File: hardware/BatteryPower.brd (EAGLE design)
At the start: 47 x 40.5 mm, 36 parts, among them U1 CH004-2032LF, U2 ACS711ELCTR-12AB-T, U3 ACS711ELCTR-12AB-T

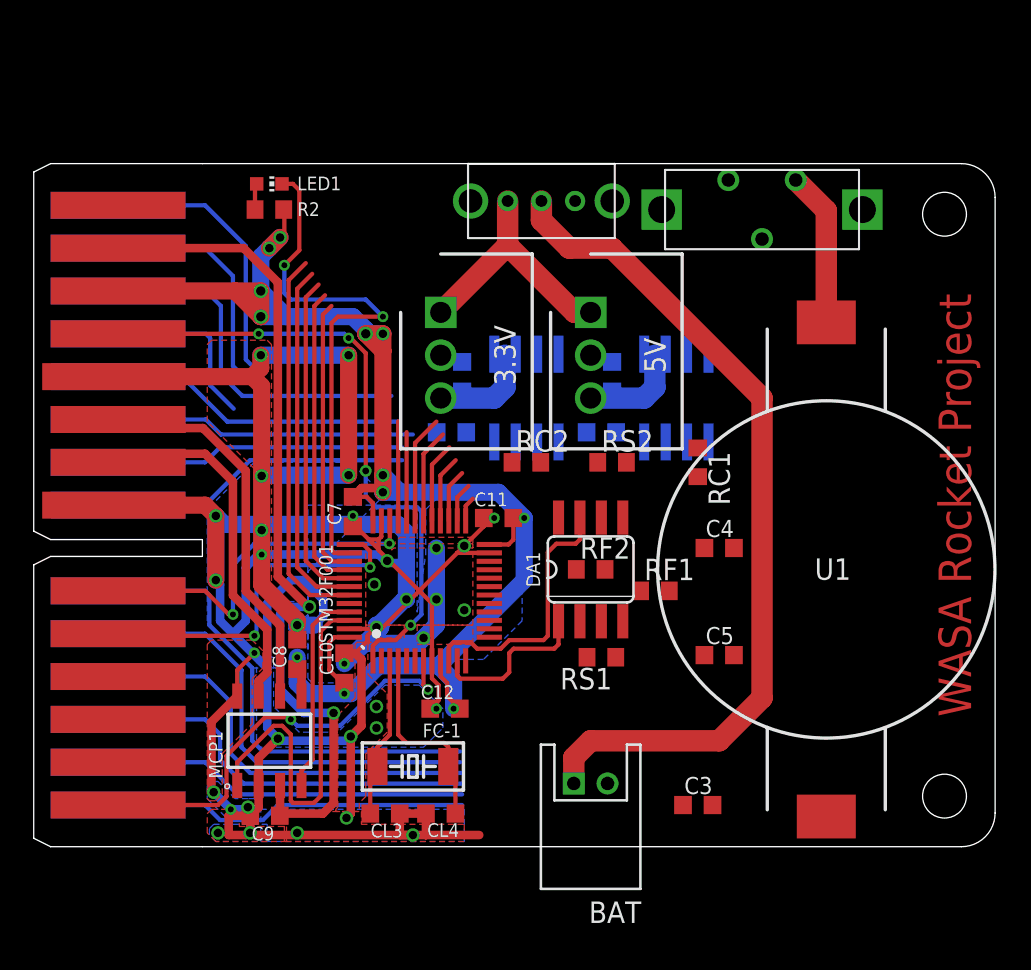
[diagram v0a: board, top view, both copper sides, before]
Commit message: Layout battery power board
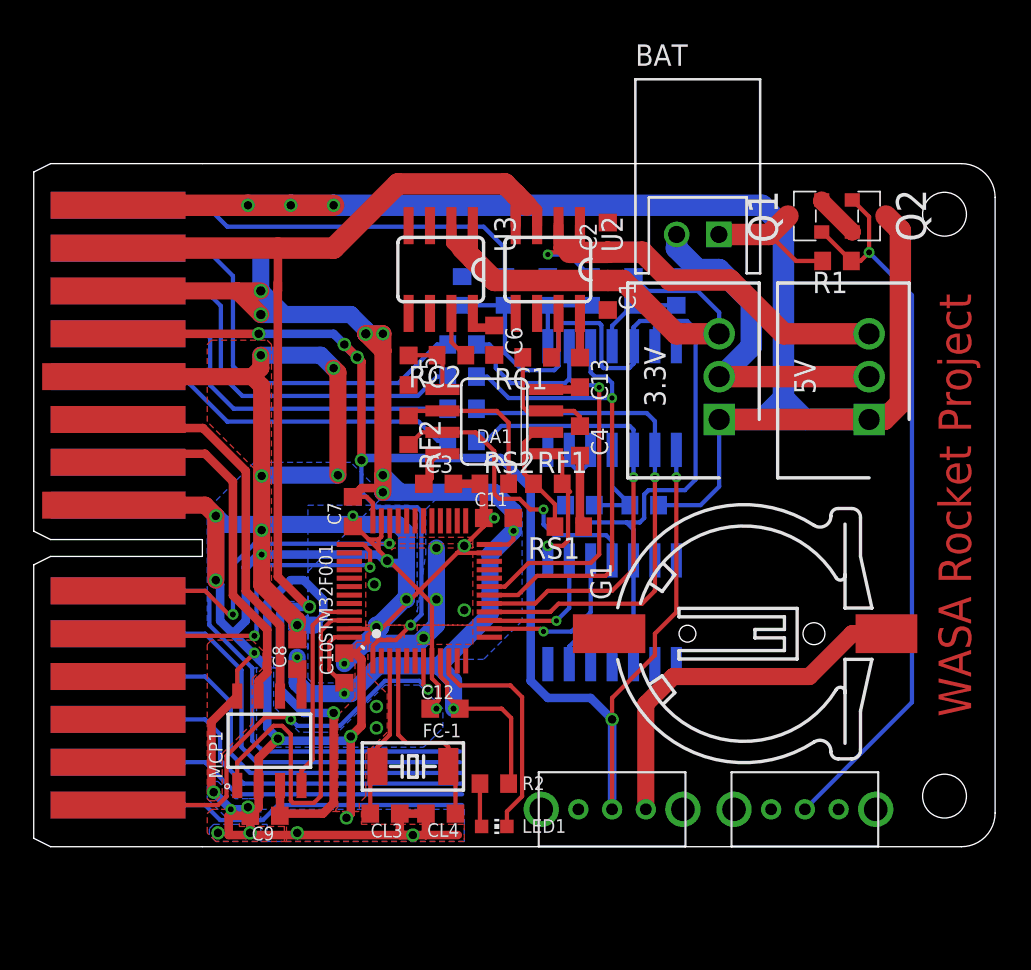
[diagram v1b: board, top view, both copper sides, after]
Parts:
- removed U$3: ESD175202, switches:ESD175202
- removed U1: CH004-2032LF, CH004-2032LF:CH004-2032LF
- added G1: CH291-1220LF, battery:CH291-1220LF
- added IC1, IC2: 4066D, 40xx:SO14
- added Q1, Q2: IRLML5203, transistor-power:MICRO3
- added R1: 100k, rcl:R0603
- added R10, R3, R5, R6, R7, R8: 10k, rcl:R0603
- added R11, R12, R13, R14, R4, R9: 1k, rcl:R0603
- added U$4: SK-12D01-VG4, switches:SK-12D01-VG4
- BAT: device jst-ph:S2B-PH-K-S -> con-jst-xh:S2B-XH-A
- moved LED1 40.4 mm to (27.3, -19.1)
- moved U$1 39.3 mm to (45.7, -18.0)
- moved R2 36.6 mm to (27.3, -16.5)
- moved BAT 33.2 mm to (39.4, 16.0), turned to 0 degrees
- moved C5 25.0 mm to (22.2, 8.00), turned to 270 degrees
- moved C3 24.5 mm to (24.0, 1.27)
- moved 3.3V 17.7 mm to (40.6, 5.08), turned to 90 degrees
- moved 5V 17.7 mm to (49.5, 5.08), turned to 90 degrees
- moved RF2 13.6 mm to (22.2, 4.45), turned to 270 degrees
- moved RC1 11.4 mm to (29.8, 8.76), turned to 180 degrees
- moved U2 10.8 mm to (30.5, 14.0), flipped to the top
- moved DA1 10.5 mm to (27.3, 4.95), turned to 90 degrees
- moved C4 10.4 mm to (32.4, 3.81), turned to 270 degrees
- moved C1 9.89 mm to (34.0, 12.4), flipped to the top, turned to 270 degrees
- moved U3 9.16 mm to (24.1, 14.0), flipped to the top
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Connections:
- net N$2 renamed 5VC'
- net N$3 renamed 3.3VC'
- removed net I2C1_SCK: STM32F001.43
- removed net I2C1_SCL: STM32F001.42
- removed net N$11: U$3.B, U1.1
- removed net N$53: STM32F001.12
- removed net N$54: STM32F001.13
- removed net N$55: STM32F001.14
- removed net N$56: STM32F001.15
- removed net N$57: STM32F001.16
- removed net N$58: STM32F001.17
- removed net N$59: STM32F001.29
- removed net N$60: STM32F001.32
- removed net N$61: STM32F001.33
- removed net N$62: STM32F001.18
- removed net N$63: STM32F001.19
- removed net N$64: STM32F001.20
- removed net N$65: STM32F001.21
- removed net N$66: STM32F001.22
- removed net N$67: STM32F001.25
- removed net N$68: STM32F001.26
- removed net N$69: STM32F001.27
- removed net N$70: STM32F001.28
- removed net N$74: U$2.16
- removed net SPI1_MISO: STM32F001.40
- removed net SPI1_MOSI: STM32F001.41
- removed net SPI1_SCK: STM32F001.39
- removed net USART1_RX: STM32F001.31
- removed net USART1_TX: STM32F001.30
- new net !HIL!: IC1.12, IC1.13, IC1.5, IC1.6, IC2.13, IC2.5, R10.1, R9.1
- new net BAT+: BAT.1, Q1.3, R1.2
- new net BU+: G1.+, U$4.B
- new net N$2: Q1.2, Q2.2
- new net POWER_CTRL: Q1.1, Q2.1, R1.1, U$1.C
- new net PVCC: IC1.8, R5.1, R6.2
- new net PVDD: IC1.11, R7.1, R8.2
- new net PVPP: IC1.4, R3.1, R4.2
- new net SCVCC: IC2.2, STM32F001.15
- new net SCVDD: IC2.3, STM32F001.14
- new net SVBU: IC1.2, R13.1, STM32F001.16
- new net SVCC: IC1.9, R11.1, STM32F001.19
- new net SVDD: IC1.10, R12.1, STM32F001.18
- new net SVPP: IC1.3, R14.1, STM32F001.17
- net 3.3V: now also R7.2
- net 3.3VC: now also IC2.4; no longer STM32F001.10
- net 5V: now also R5.2
- net 5VC: now also IC2.1; no longer STM32F001.11
- net GND: now also G1.-, IC1.7, IC2.7, R4.1, R6.1, R8.1, U$1.B; no longer U1.2
- net N$1: now also R9.2, U$2.16; no longer 3.3V.1, 5V.1, U$1.B
- net N$48: now also R14.2
- net N$49: now also R13.2
- net N$50: now also R12.2
- net N$73: now also STM32F001.10; no longer STM32F001.38
- net N$75: now also R11.2
- net VBAT: now also IC1.1, U$4.C; no longer U$3.C
- net VDD: now also IC1.14, IC2.14, R10.2
- net VPP: now also 3.3V.1, 5V.1, Q2.3, R3.2; no longer BAT.1, U$1.C
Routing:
- net !HIL!: track 0.00 -> 61.9 mm
- net VBAT: track 38.0 -> 94.9 mm, vias 4 -> 7
- net VPP: track 50.5 -> 102.1 mm, vias 0 -> 3
- net POWER_CTRL: track 0.00 -> 44.0 mm, vias 0 -> 1
- net SVBU: track 0.00 -> 31.3 mm, vias 0 -> 1
- net SVDD: track 0.00 -> 30.6 mm, vias 0 -> 1
- net SVCC: track 0.00 -> 28.3 mm, vias 0 -> 1
- net GND: track 213.4 -> 241.1 mm
- net SVPP: track 0.00 -> 27.4 mm, vias 0 -> 1
- net I2C1_SCK: track 23.0 -> 0.00 mm
- net 5V: track 5.98 -> 28.5 mm, vias 0 -> 1
- net 3.3V: track 5.98 -> 28.4 mm
- net BU+: track 0.00 -> 22.2 mm
- net VCC: track 51.1 -> 73.2 mm
- net I2C1_SCL: track 21.3 -> 0.00 mm
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
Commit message: Complete battery power board
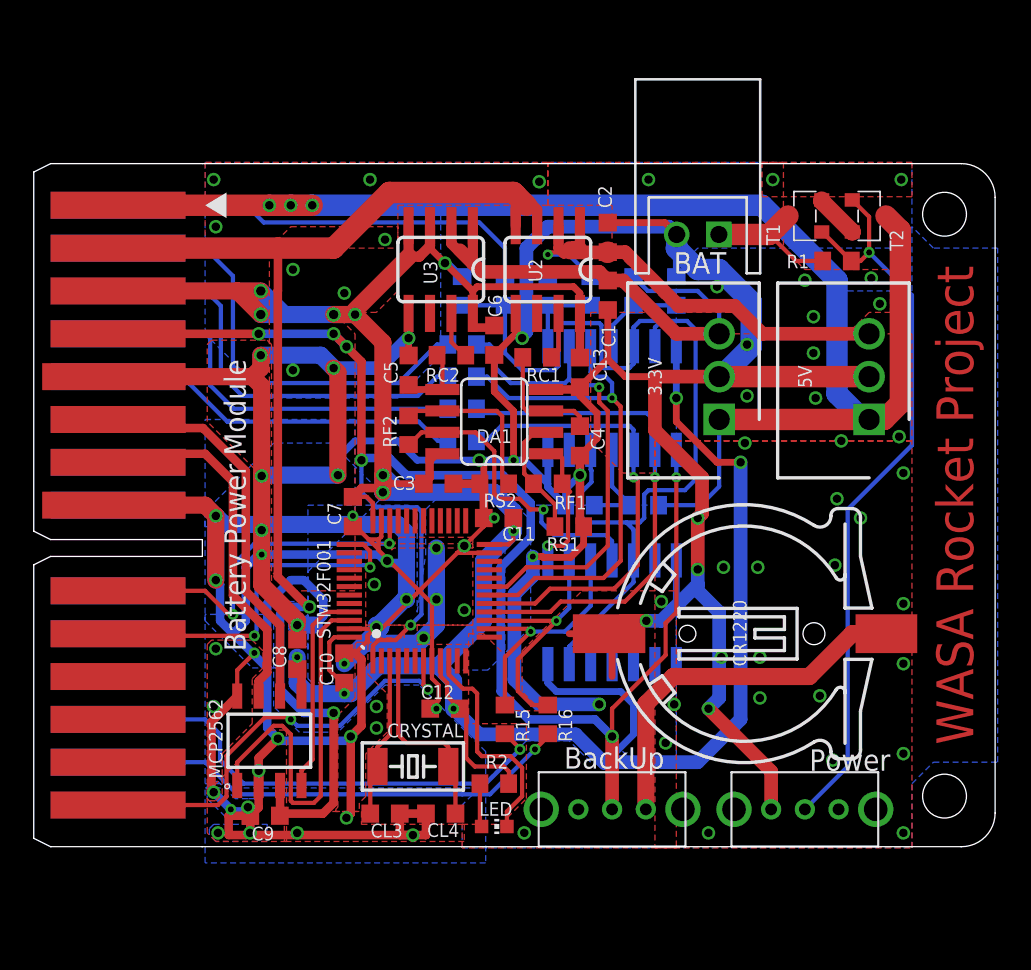
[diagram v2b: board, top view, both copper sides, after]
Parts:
- added R15, R16: 1k, resistor:R0603
- turned C5 to 90 degrees
- renumbered FC-1 to CRYSTAL, G1 to CR1220, LED1 to LED, MCP1 to MCP2562, Q1 to T1, Q2 to T2, U$4 to BACKUP
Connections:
- removed net N$33: U$2.30
- removed net N$36: U$2.27
- removed net N$43: U$2.26
- removed net N$44: U$2.25
- removed net N$45: U$2.23
- removed net N$46: U$2.22
- removed net N$47: U$2.21
- net N$34: now also R16.2
- net N$35: now also R15.2
- net SCVCC: now also R16.1
- net SCVDD: now also R15.1
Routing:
- net GND: track 241.1 -> 381.6 mm, vias 35 -> 91
- net VDD: track 103.1 -> 179.8 mm, vias 10 -> 13
- net N$44: track 27.8 -> 0.00 mm
- net N$43: track 26.1 -> 0.00 mm
- net N$36: track 24.6 -> 0.00 mm
- net N$33: track 21.1 -> 0.00 mm
- net VPP: track 102.1 -> 86.9 mm
- net SCVCC: track 7.89 -> 15.1 mm
- net N$34: track 21.2 -> 27.9 mm, vias 0 -> 1
- net N$35: track 22.9 -> 28.4 mm, vias 0 -> 1
- net SCVDD: track 9.62 -> 14.4 mm
- net VBAT: track 94.9 -> 92.3 mm
- net VCC: track 73.2 -> 72.3 mm
- net SVBU: track 31.3 -> 30.6 mm
- net !HIL!: track 61.9 -> 61.3 mm
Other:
- board text added: "BackUp"
- board text added: "Battery Power Module"
- board text added: "Designed by @fujiy0, 2019"
- board text added: "Power"

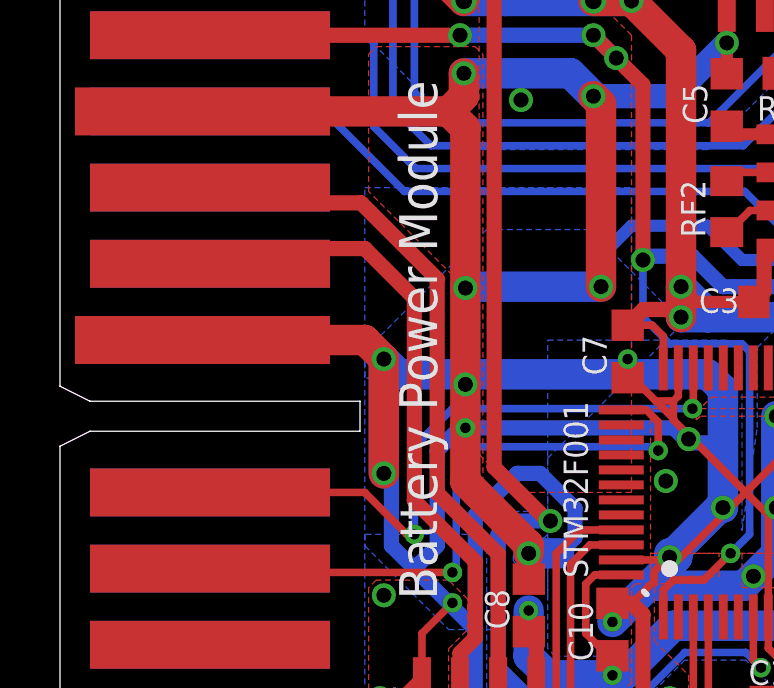
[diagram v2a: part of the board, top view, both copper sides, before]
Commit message: Clean silk print
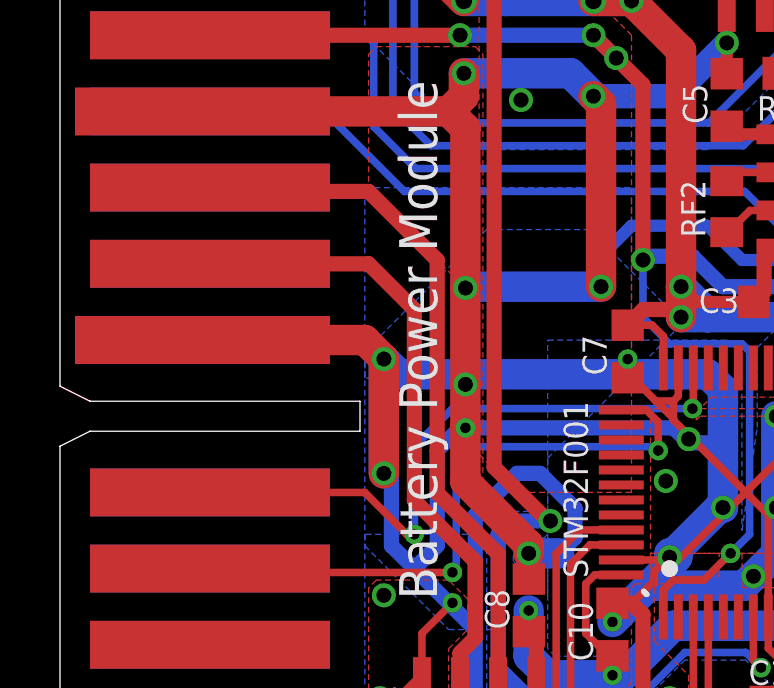
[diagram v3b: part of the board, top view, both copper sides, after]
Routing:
- net CANH1: track 21.5 -> 20.8 mm
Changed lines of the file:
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@@
 <layer number="28" name="bValues" color="7" fill="1" visible="no" active="yes"/>
 <layer number="29" name="tStop" color="7" fill="3" visible="no" active="yes"/>
-<layer number="30" name="bStop" color="7" fill="6" visible="yes" active="yes"/>
+<layer number="30" name="bStop" color="7" fill="6" visible="no" active="yes"/>
 <layer number="31" name="tCream" color="7" fill="4" visible="no" active="yes"/>
 <layer number="32" name="bCream" color="7" fill="5" visible="no" active="yes"/>
@@
 <contactref element="U$2" pad="7"/>
 <contactref element="MCP2562" pad="7"/>
-<wire x1="11.811" y1="1.397" x2="11.811" y2="-5.351" width="0.508" layer="1"/>
+<wire x1="11.811" y1="1.016" x2="11.811" y2="-5.351" width="0.508" layer="1"/>
 <wire x1="13.843" y1="-7.383" x2="13.843" y2="-9.923" width="0.508" layer="1"/>
 <wire x1="13.843" y1="-9.923" x2="13.335" y2="-10.431" width="0.508" layer="1"/>
 <wire x1="13.335" y1="-11.32" x2="13.335" y2="-10.431" width="0.508" layer="1"/>
 <wire x1="13.843" y1="-7.383" x2="11.811" y2="-5.351" width="0.508" layer="1"/>
-<wire x1="11.811" y1="1.397" x2="10.16" y2="3.048" width="0.508" layer="1"/>
-<wire x1="10.16" y1="3.048" x2="5.508" y2="3.048" width="0.508" layer="1"/>
-<wire x1="5.508" y1="3.048" x2="5" y2="2.54" width="0.508" layer="1"/>
+<wire x1="11.811" y1="1.016" x2="10.287" y2="2.54" width="0.508" layer="1"/>
+<wire x1="10.287" y1="2.54" x2="5" y2="2.54" width="0.508" layer="1"/>
 </signal>
 <signal name="VBAT">
@@
 <wire x1="14.605" y1="-11.32" x2="14.605" y2="-7.129" width="0.508" layer="1"/>
 <wire x1="14.605" y1="-7.129" x2="12.573" y2="-5.097" width="0.508" layer="1"/>
-<wire x1="12.573" y1="2.032" x2="12.573" y2="-5.097" width="0.508" layer="1"/>
-<wire x1="12.573" y1="2.032" x2="10.033" y2="4.572" width="0.508" layer="1"/>
-<wire x1="10.033" y1="4.572" x2="5.508" y2="4.572" width="0.508" layer="1"/>
-<wire x1="5.508" y1="4.572" x2="5" y2="5.08" width="0.508" layer="1"/>
+<wire x1="12.573" y1="2.667" x2="12.573" y2="-5.097" width="0.508" layer="1"/>
+<wire x1="12.573" y1="2.667" x2="10.287" y2="4.953" width="0.508" layer="1"/>
+<wire x1="10.287" y1="4.953" x2="5.127" y2="4.953" width="0.508" layer="1"/>
+<wire x1="5.127" y1="4.953" x2="5" y2="5.08" width="0.508" layer="1"/>
 </signal>
 <signal name="CAN_RX">
